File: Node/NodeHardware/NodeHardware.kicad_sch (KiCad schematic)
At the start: 72 parts, among them J1 USB_C_Receptacle_16P, J10 PWR_OUT_5V, J11 PWR_OUT_3V3, J2 CONN_I2C, J3 ESP32_JTAG, J4 PWR_IN, J5 BATT, J6 CONN_SPI, J7 DIG_IO_A, J8 DIG_IO_B, J9 ANA_IN, Q1 AO3401A, Q2 AO3401A, U1 TPS565201DDCR, U2 SPX3819M5-L-3-3, U3 CH340C, U5 MCP73831-2-OT, U9 SIM7000G_DEVBoard

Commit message: Never ending SCHM design
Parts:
- removed J11: PWR_OUT_3V3, symbol Connector_Generic:Conn_01x04
- removed J6: CONN_SPI, symbol Connector_Generic:Conn_01x07
- removed J7: DIG_IO_A, symbol Connector_Generic:Conn_01x06
- removed J8: DIG_IO_B, symbol Connector_Generic:Conn_01x06
- removed J9: ANA_IN, symbol Connector_Generic:Conn_01x08
- removed U9: SIM7000G_DEVBoard, fflori4nComponents:sim7000G_dev_board_rev3, symbol myComponents:SIM7000G_DEVBoard
- added J1: PWR_OUT_5V, fflori4nComponents:TerminalBlockRemovablex6, symbol Connector_Generic:Conn_01x06
- added J11: DIG_IO_04, fflori4nComponents:TerminalBlockRemovablex2_Silk, symbol Connector_Generic:Conn_01x02
- added J12: DIG_IO_05, fflori4nComponents:TerminalBlockRemovablex2_Silk, symbol Connector_Generic:Conn_01x02
- added J13: DIG_IO_06, fflori4nComponents:TerminalBlockRemovablex2_Silk, symbol Connector_Generic:Conn_01x02
- added J14, J15, J16, J17: ANA_IN_01, fflori4nComponents:TerminalBlockRemovablex2_Silk, symbol Connector_Generic:Conn_01x02
- added J19: CONN_SPI, fflori4nComponents:TerminalBlockRemovablex6, symbol Connector_Generic:Conn_01x06
- added J2: PWR_OUT_3V3, fflori4nComponents:TerminalBlockRemovablex6, symbol Connector_Generic:Conn_01x06
- added J20: DIG_OUT_01, fflori4nComponents:TerminalBlockRemovablex2_Silk, symbol Connector_Generic:Conn_01x02
- added J21: DIG_OUT_02, fflori4nComponents:TerminalBlockRemovablex2_Silk, symbol Connector_Generic:Conn_01x02
- added J6: DIG_IO_01, fflori4nComponents:TerminalBlockRemovablex2_Silk, symbol Connector_Generic:Conn_01x02
- added J7: DIG_IO_02, fflori4nComponents:TerminalBlockRemovablex2_Silk, symbol Connector_Generic:Conn_01x02
- added J8: DIG_IO_03, fflori4nComponents:TerminalBlockRemovablex2_Silk, symbol Connector_Generic:Conn_01x02
- added R14: 0R, Resistor_SMD:R_0805_2012Metric, symbol Device:R
- added U5: SIM7000G_DEVBoard, fflori4nComponents:sim7000G_dev_board_rev3, symbol fflori4nComponents:SIM7000G_DEVBoard
- D2: value 5V1 -> 3v3
- J10: value PWR_OUT_5V -> PWR_OUT_GND; footprint (none) -> fflori4nComponents:TerminalBlockRemovablex4
- J18: renamed from J2; footprint (none) -> fflori4nComponents:TerminalBlockRemovablex2
- J3: renamed from J4; footprint fflori4nComponents:TerminalBlockRemovablex2_Silk -> fflori4nComponents:TerminalBlockRemovablex2
- J4: renamed from J5; footprint fflori4nComponents:TerminalBlockRemovablex2_Silk -> fflori4nComponents:TerminalBlockRemovablex2
- J9: renamed from J3; footprint (none) -> Connector_PinHeader_2.54mm:PinHeader_1x07_P2.54mm_Vertical
- renumbered C2 to C1, C7 to C10, C14 to C11, C36 to C13, C37 to C14, C38 to C15, C3 to C2, C16 to C3, C13 to C5, C15 to C6, C1 to C7, C5 to C8, C6 to C9, D3 to D1, D4 to D3, D1 to D4, H3 to H2, H2 to H3, J1 to J5, R5 to R1, R24 to R10, R3 to R11, R7 to R12, R8 to R13, R6 to R15, R18 to R17, R14 to R18, R20 to R19, R23 to R2, R21 to R20, R13 to R21, R17 to R22, R19 to R23, R1 to R3, R22 to R4, R2 to R5, R4 to R6, R25 to R7, R27 to R8, R15 to R9, TP7 to TP2, TP2 to TP3, TP8 to TP4, TP3 to TP5, TP4 to TP6, TP5 to TP7, TP6 to TP8, U5 to U1, U1 to U2, U2 to U3, U3 to U4
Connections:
- net +3V3: now also J19.6 (Pin_6), J2.1 (Pin_1), J2.2 (Pin_2), J2.3 (Pin_3), J2.4 (Pin_4), J2.5 (Pin_5), J2.6 (Pin_6), U5.7 (V_MCU)
- net +5V: now also J1.1 (Pin_1), J1.2 (Pin_2), J1.3 (Pin_3), J1.4 (Pin_4), J1.5 (Pin_5), J1.6 (Pin_6), R14.2, U5.2 (POWER); no longer J10.1 (Pin_1), J10.2 (Pin_2), J10.3 (Pin_3), J10.4 (Pin_4), L1.2, R11.1
- net ANA_IN_01: now also J14.2 (Pin_2)
- net ANA_IN_02: now also J15.2 (Pin_2)
- net ANA_IN_03: now also J16.2 (Pin_2)
- net ANA_IN_04: now also J17.2 (Pin_2)
- net DIG_IO_01: now also J6.2 (Pin_2)
- net DIG_IO_02: now also J7.2 (Pin_2)
- net DIG_IO_03: now also J8.2 (Pin_2)
- net DIG_IO_04: now also J11.2 (Pin_2)
- net DIG_IO_05: now also J12.2 (Pin_2)
- net DIG_IO_06: now also J13.2 (Pin_2)
- net GND: now also J10.1 (Pin_1), J10.2 (Pin_2), J10.3 (Pin_3), J10.4 (Pin_4), J11.1 (Pin_1), J12.1 (Pin_1), J13.1 (Pin_1), J14.1 (Pin_1), J15.1 (Pin_1), J16.1 (Pin_1), J17.1 (Pin_1), J19.1 (Pin_1), J20.1 (Pin_1), J21.1 (Pin_1), J6.1 (Pin_1), J7.1 (Pin_1), J8.1 (Pin_1), U5.3 (GND), U5.5 (GND)
- net SPI_MISO: now also J19.4 (Pin_4)
- net SPI_MOSI: now also J19.3 (Pin_3)
- net SPI_SCLK: now also J19.2 (Pin_2)
- net UART1_UC_RX: now also U5.8 (TXD)
- net UART1_UC_TX: now also U5.6 (RXD)
- new net: L1.2, R11.1, R14.1
- new net DIG_OUT_01: J20.2 (Pin_2)
- new net DIG_OUT_02: J21.2 (Pin_2)
- new net SPI_CS_EXT: J19.5 (Pin_5)
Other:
- note added: "Digital Open Drain Outputs"
- note added: "Ground"
- note added: "Supplies"
- moved on the sheet: J9, TP3

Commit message: Halfway working on PCB for Node
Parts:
- added N1: Housing, PlasticEnclosures:PlasticEnclosure_150x110x70, symbol Mechanical:Housing
- added TP11: TP_BATT_PROT, TestPoint:TestPoint_Pad_D2.0mm, symbol Connector:TestPoint
- added TP12: TP_3V3, TestPoint:TestPoint_Pad_D2.0mm, symbol Connector:TestPoint
- added TP13: TP_5V, TestPoint:TestPoint_Pad_D2.0mm, symbol Connector:TestPoint
- C1, C13, C14, C8: footprint (none) -> Capacitor_SMD:CP_Elec_6.3x7.7
- J1, J19, J2: footprint fflori4nComponents:TerminalBlockRemovablex6 -> TerminalBlock:TerminalBlock_bornier-6_P5.08mm
- J10: footprint fflori4nComponents:TerminalBlockRemovablex4 -> TerminalBlock:TerminalBlock_bornier-4_P5.08mm
- J11, J12, J13, J14, J15, J16, J17, J20, J21, J6, J7, J8: footprint fflori4nComponents:TerminalBlockRemovablex2_Silk -> TerminalBlock:TerminalBlock_bornier-2_P5.08mm
- J18: footprint fflori4nComponents:TerminalBlockRemovablex2 -> TerminalBlock:TerminalBlock_bornier-4_P5.08mm
- L1: footprint (none) -> Inductor_SMD:L_6.3x6.3_H3
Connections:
- net +3V3: now also TP12.1
- net +5V: now also TP13.1
- net +BATT: now also TP11.1
- net JTAG_RST renamed RST
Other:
- note added: "BATT_N"
- note added: "PWR_IN_N"
- moved on the sheet: C12, C13, C14, C15, H1, H2, H3, H4, J1, J10, J11, J12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

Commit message: Continue updating PCB (main form)
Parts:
- removed H4: MountingHole, MountingHole:MountingHole_3.2mm_M3_Pad_Via, symbol Mechanical:MountingHole_Pad
- removed J1: PWR_OUT_5V, TerminalBlock:TerminalBlock_bornier-6_P5.08mm, symbol Connector_Generic:Conn_01x06
- removed J10: PWR_OUT_GND, TerminalBlock:TerminalBlock_bornier-4_P5.08mm, symbol Connector_Generic:Conn_01x04
- removed J12: DIG_IO_05, TerminalBlock:TerminalBlock_bornier-2_P5.08mm, symbol Connector_Generic:Conn_01x02
- removed J13: DIG_IO_06, TerminalBlock:TerminalBlock_bornier-2_P5.08mm, symbol Connector_Generic:Conn_01x02
- removed J2: PWR_OUT_3V3, TerminalBlock:TerminalBlock_bornier-6_P5.08mm, symbol Connector_Generic:Conn_01x06
- added H1: MountingHole, MountingHole:MountingHole_3.2mm_M3_Pad_Via, symbol Mechanical:MountingHole_Pad
- added J12: PWR_OUT, TerminalBlock:TerminalBlock_bornier-4_P5.08mm, symbol Connector_Generic:Conn_01x04
- J11: renamed from J15; value ANA_IN_01 -> ANA_IN_02
- J15: renamed from J16; value ANA_IN_01 -> ANA_IN_03
- J17: value ANA_IN_01 -> ANA_IN_04
- J4: renamed from J3; footprint fflori4nComponents:TerminalBlockRemovablex2 -> TerminalBlock:TerminalBlock_bornier-2_P5.08mm
- J6: renamed from J4; footprint fflori4nComponents:TerminalBlockRemovablex2 -> TerminalBlock:TerminalBlock_bornier-2_P5.08mm
- renumbered C7 to C1, C14 to C10, C15 to C11, C5 to C12, C11 to C13, C6 to C14, C3 to C15, C1 to C2, C2 to C3, C8 to C5, C9 to C6, C10 to C7, C12 to C8, C13 to C9, D2 to D1, D4 to D2, D1 to D3, D3 to D4, H1 to H2, H2 to H4, J18 to J1, J8 to J10, J7 to J13, J11 to J14, J21 to J16, J5 to J2, J19 to J3, J9 to J5, J14 to J7, J20 to J8, J6 to J9, R3 to R1, R21 to R10, R16 to R11, R17 to R12, R22 to R13, R23 to R14, R19 to R15, R20 to R16, R4 to R17, R9 to R18, R13 to R19, R14 to R2, R2 to R20, R10 to R21, R7 to R22, R8 to R23, R5 to R3, R11 to R4, R6 to R5, R1 to R6, R15 to R7, R12 to R8, R18 to R9, TP5 to TP1, TP4 to TP10, TP2 to TP11, TP6 to TP2, TP7 to TP3, TP8 to TP4, TP1 to TP5, TP3 to TP6, TP13 to TP7, TP11 to TP8, TP12 to TP9, U2 to U1, U4 to U2, U5 to U3, U3 to U4, U1 to U5
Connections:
- net +3V3: now also J12.2 (Pin_2)
- net +5V: now also J12.3 (Pin_3)
- net GND: now also H1.1, J12.1 (Pin_1)
- net V_IN: now also J12.4 (Pin_4)
- no-connect marks 11 -> 12
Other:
- note added: "Power Supplies"
- note removed: "Ground"
- note removed: "Supplies"
- moved on the sheet: H2, H4, J10, J13, J14, J5, J9

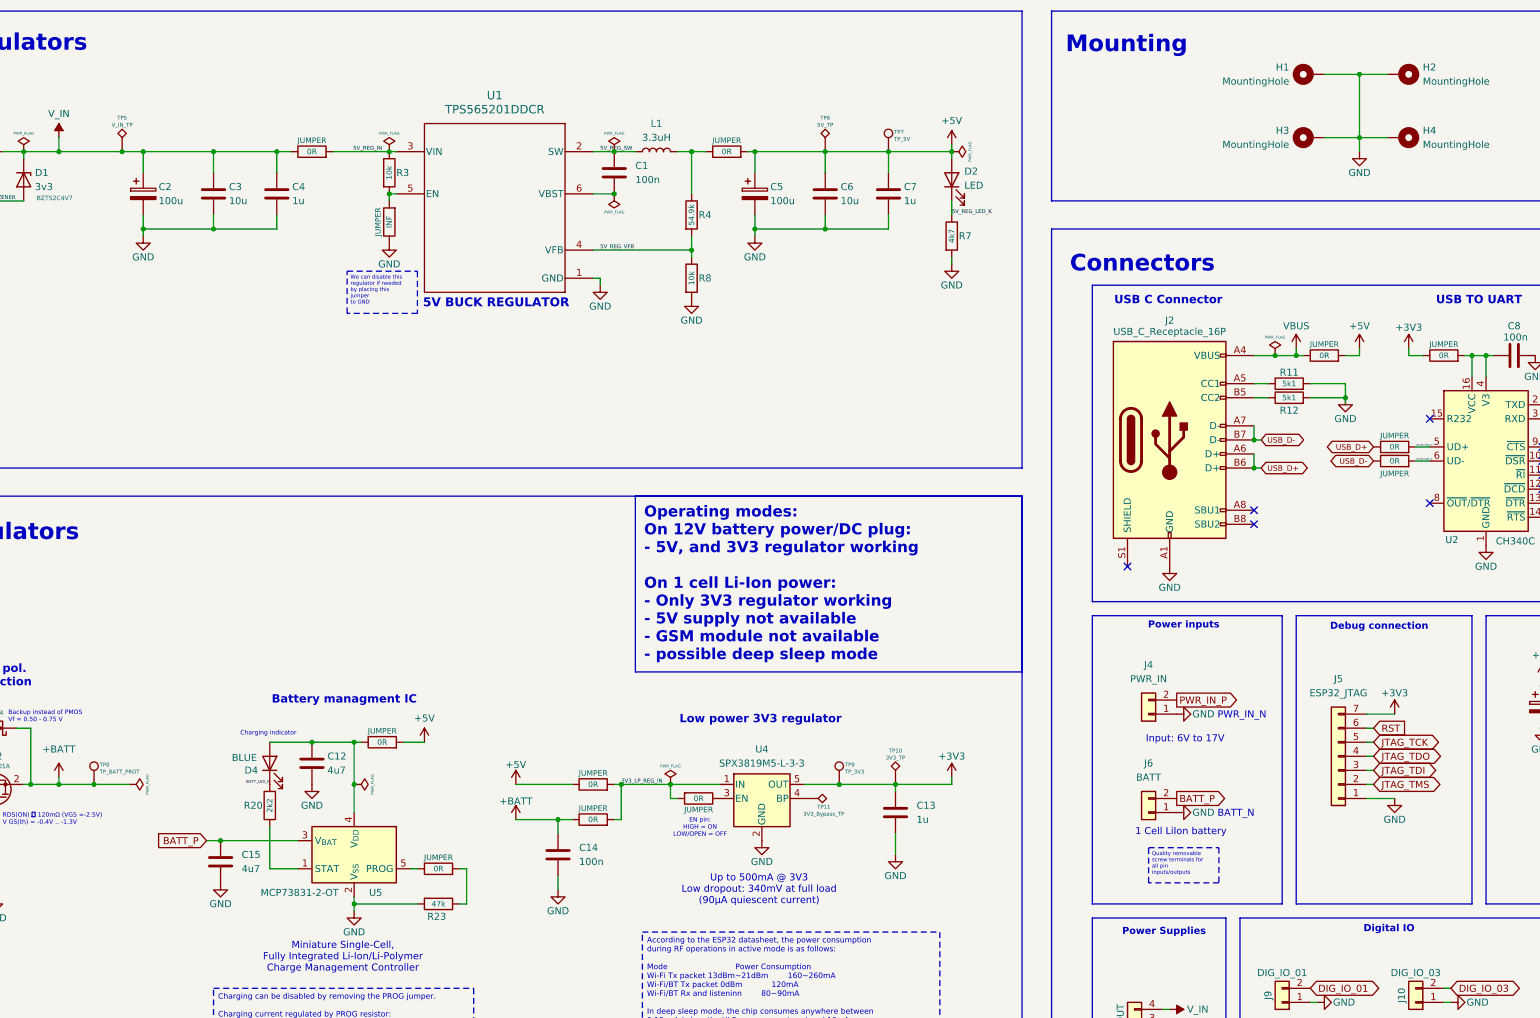
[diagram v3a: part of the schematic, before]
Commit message: Finish v1 of PCB layout
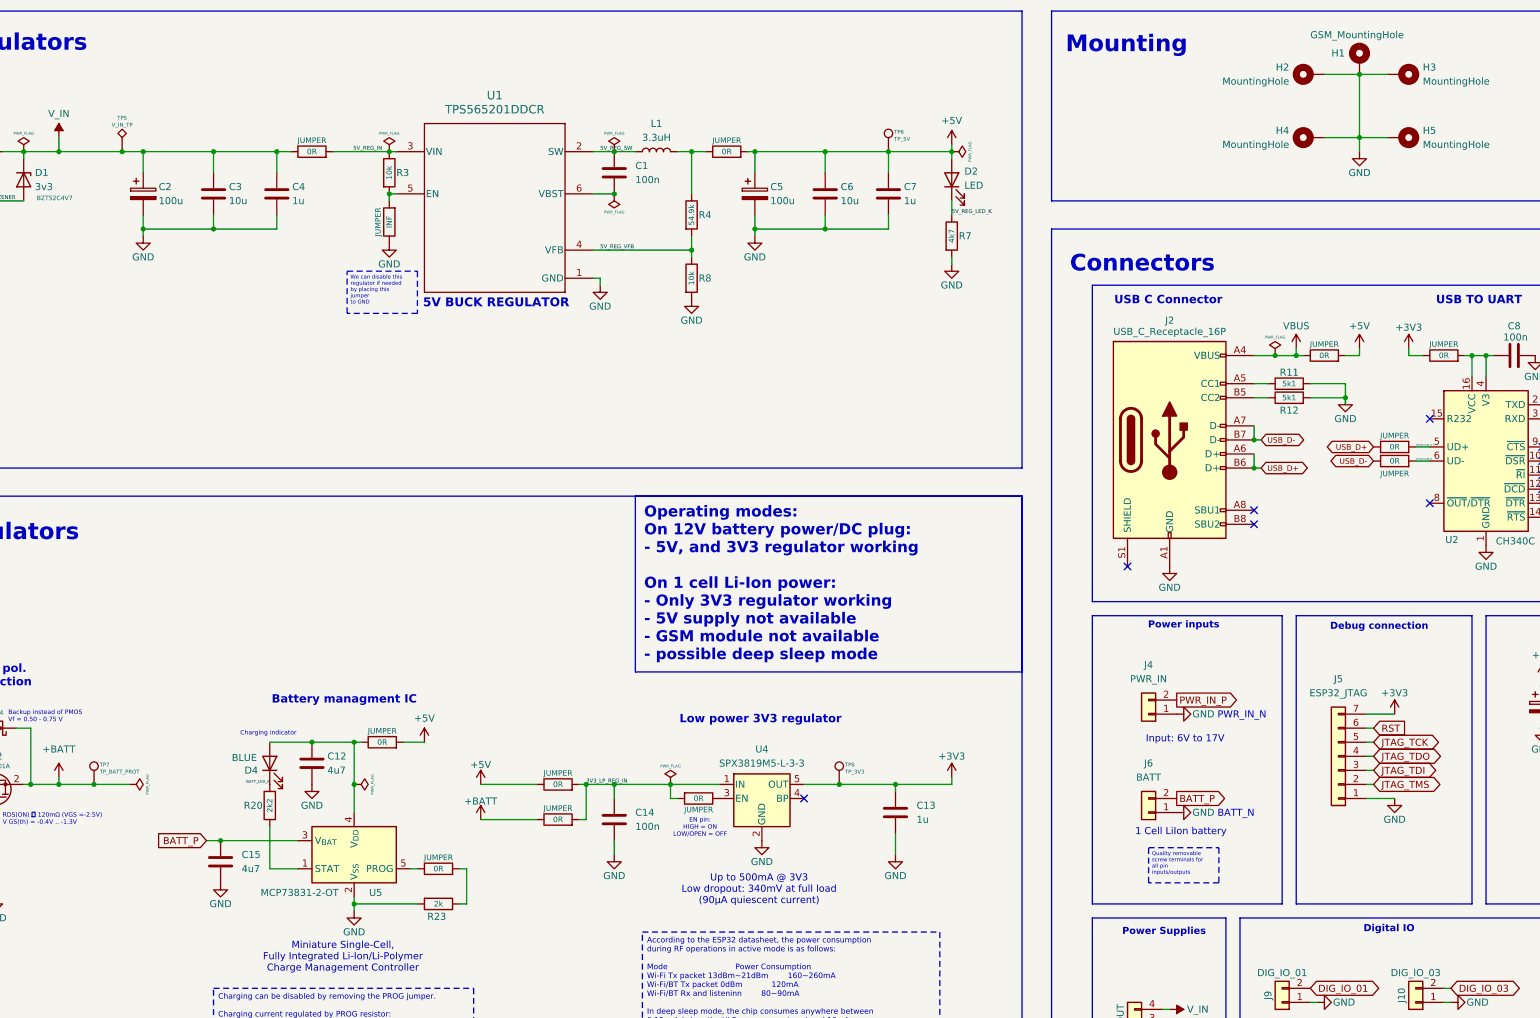
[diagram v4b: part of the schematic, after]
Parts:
- removed TP10: 3V3_TP, TestPoint:TestPoint_Pad_D2.0mm, symbol Connector:TestPoint_Alt
- removed TP11: 3V3_Bypass_TP, TestPoint:TestPoint_Pad_D2.0mm, symbol Connector:TestPoint_Alt
- removed TP6: 5V_TP, TestPoint:TestPoint_Pad_D2.0mm, symbol Connector:TestPoint_Alt
- added H1: GSM_MountingHole, MountingHole:MountingHole_3.2mm_M3_Pad_Via, symbol Mechanical:MountingHole_Pad
- R23: value 47k -> 2k
- renumbered H1 to H2, H2 to H3, H3 to H4, H4 to H5, TP7 to TP6, TP8 to TP7, TP9 to TP8
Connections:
- net +BATT: no longer C14.1
- net 3V3_LP_REG_IN: now also C14.1
- net GND: now also H1.1
- no-connect marks 12 -> 13
